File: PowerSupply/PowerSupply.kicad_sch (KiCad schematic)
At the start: 19 parts, among them J1 Conn_01x01_Socket, J2 Conn_01x01_Socket, J3 Conn_01x03_Pin, U1 LM317_SOT-223, U2 LM337_SOT223

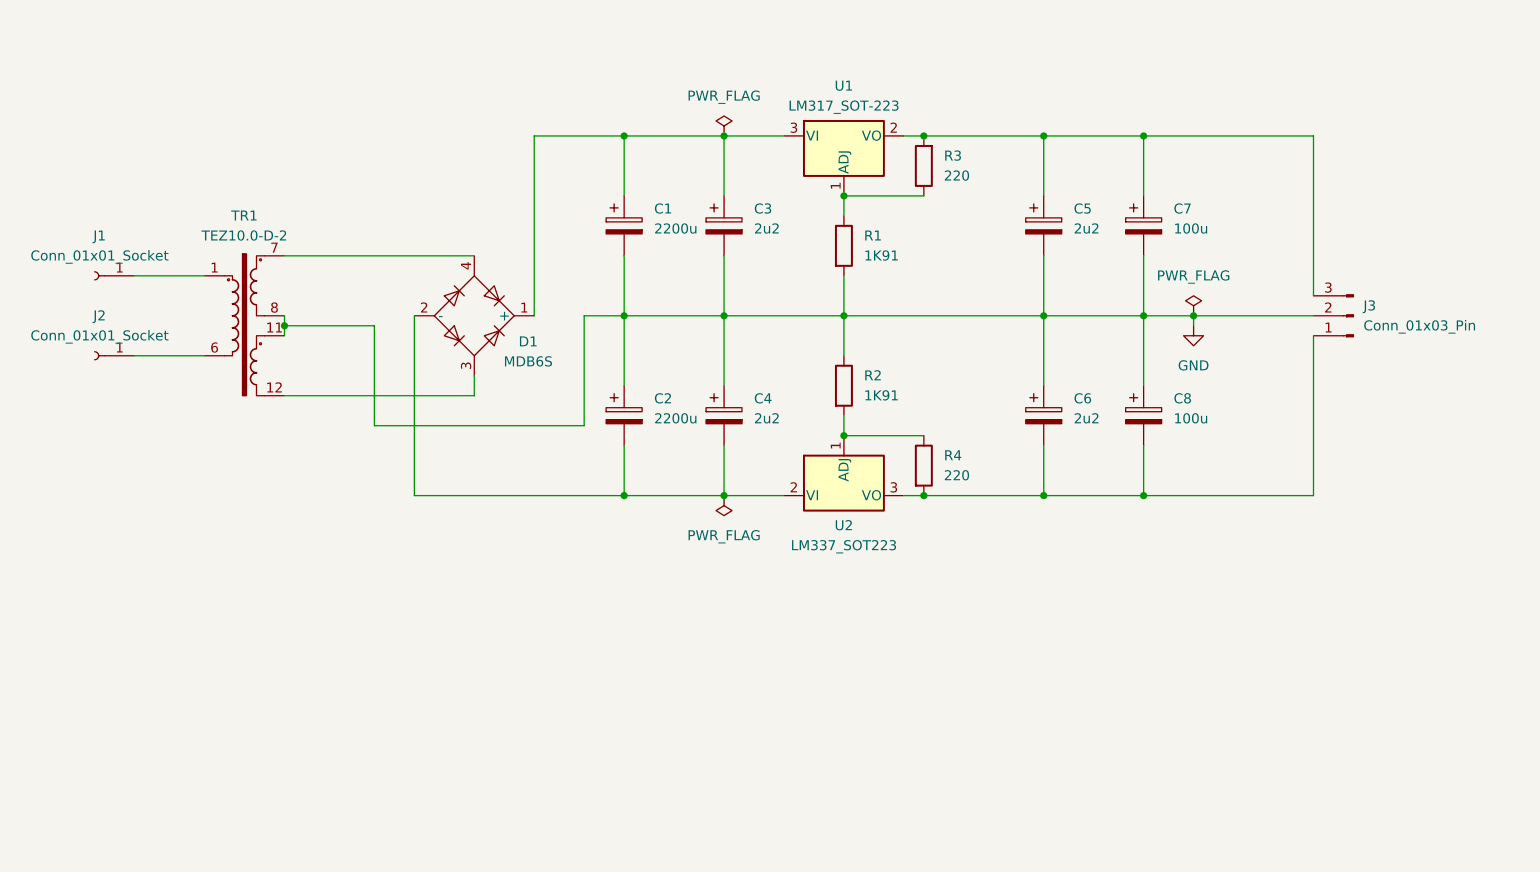
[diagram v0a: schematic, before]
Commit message: Project Structure
Updated the project structure.
Added a preamplifier project.
Added a power supply project.
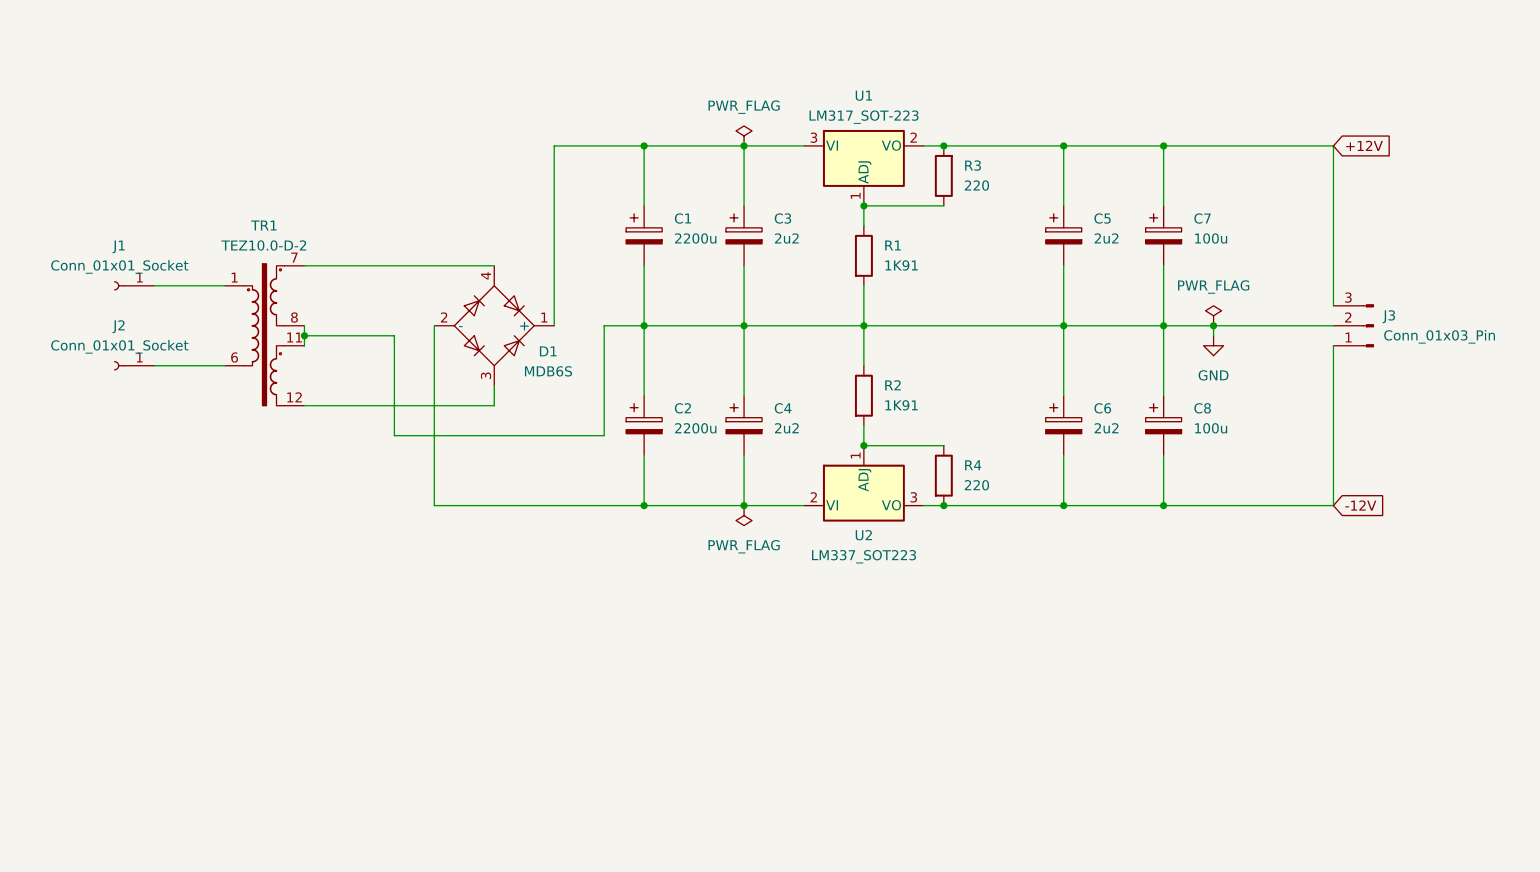
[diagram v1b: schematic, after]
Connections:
- net +12V: now reaches C5.1, C7.1, J3.3 (Pin_3), R3.2, U1.2 (VO)
- net -12V: now reaches C6.2, C8.2, J3.1 (Pin_1), R4.2, U2.3 (VO)
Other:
- moved on the sheet: C1, C2, C3, C4, C5, C6, C7, C8, D1, J1, J2, J3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

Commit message: READY FOR MANUFACTURING v3
preamplifier:
updated silkscreen
PS ready to manufacturing
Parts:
- added D2, D3: SM4001, Diode_SMD:D_SMA, symbol Diode:SM4001
- added H1, H2, H3, H4: MountingHole, MountingHole:MountingHole_3.2mm_M3, symbol Mechanical:MountingHole
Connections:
- net +12V: now also J3.1 (Pin_1), D2.2 (A); no longer J3.3 (Pin_3)
- net -12V: now also J3.3 (Pin_3), D3.1 (K); no longer J3.1 (Pin_1)
- net at C1.1, C3.1, D1.1 (+)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: now also D2.1 (K)
- net at C2.2, C4.2, D1.2 (-)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: now also D3.2 (A)
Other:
- moved on the sheet: J3
